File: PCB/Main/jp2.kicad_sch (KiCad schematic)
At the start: 1 part, among them U1 ORANGE_PI_CM4

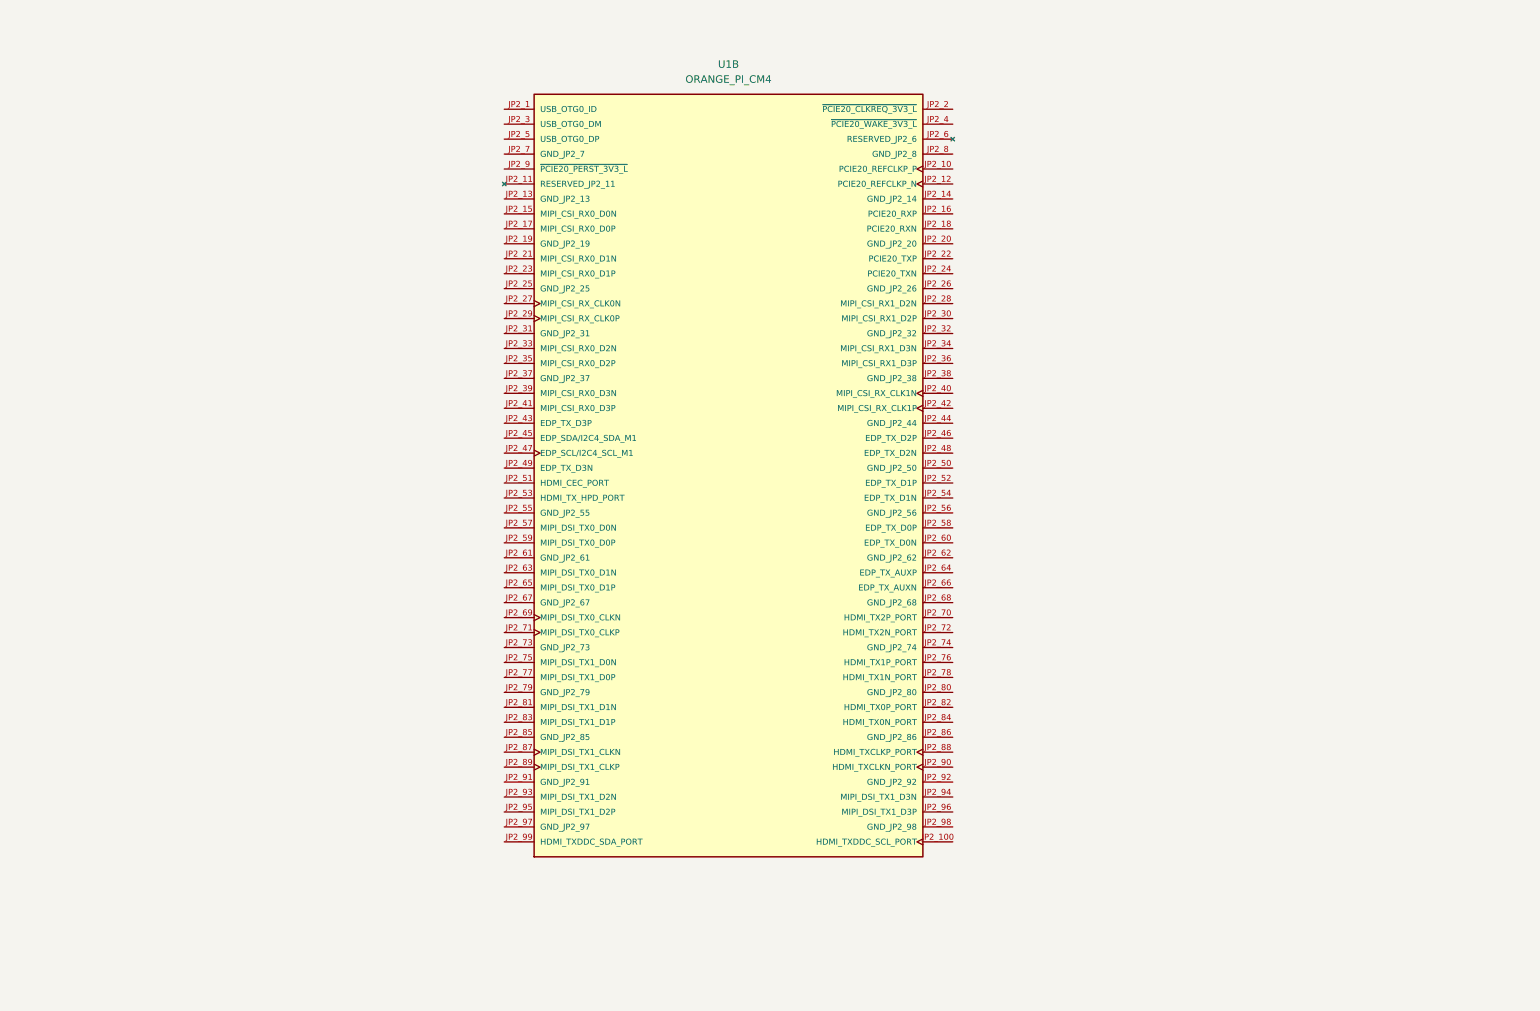
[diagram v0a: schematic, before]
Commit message: renaming y basico sin pcb
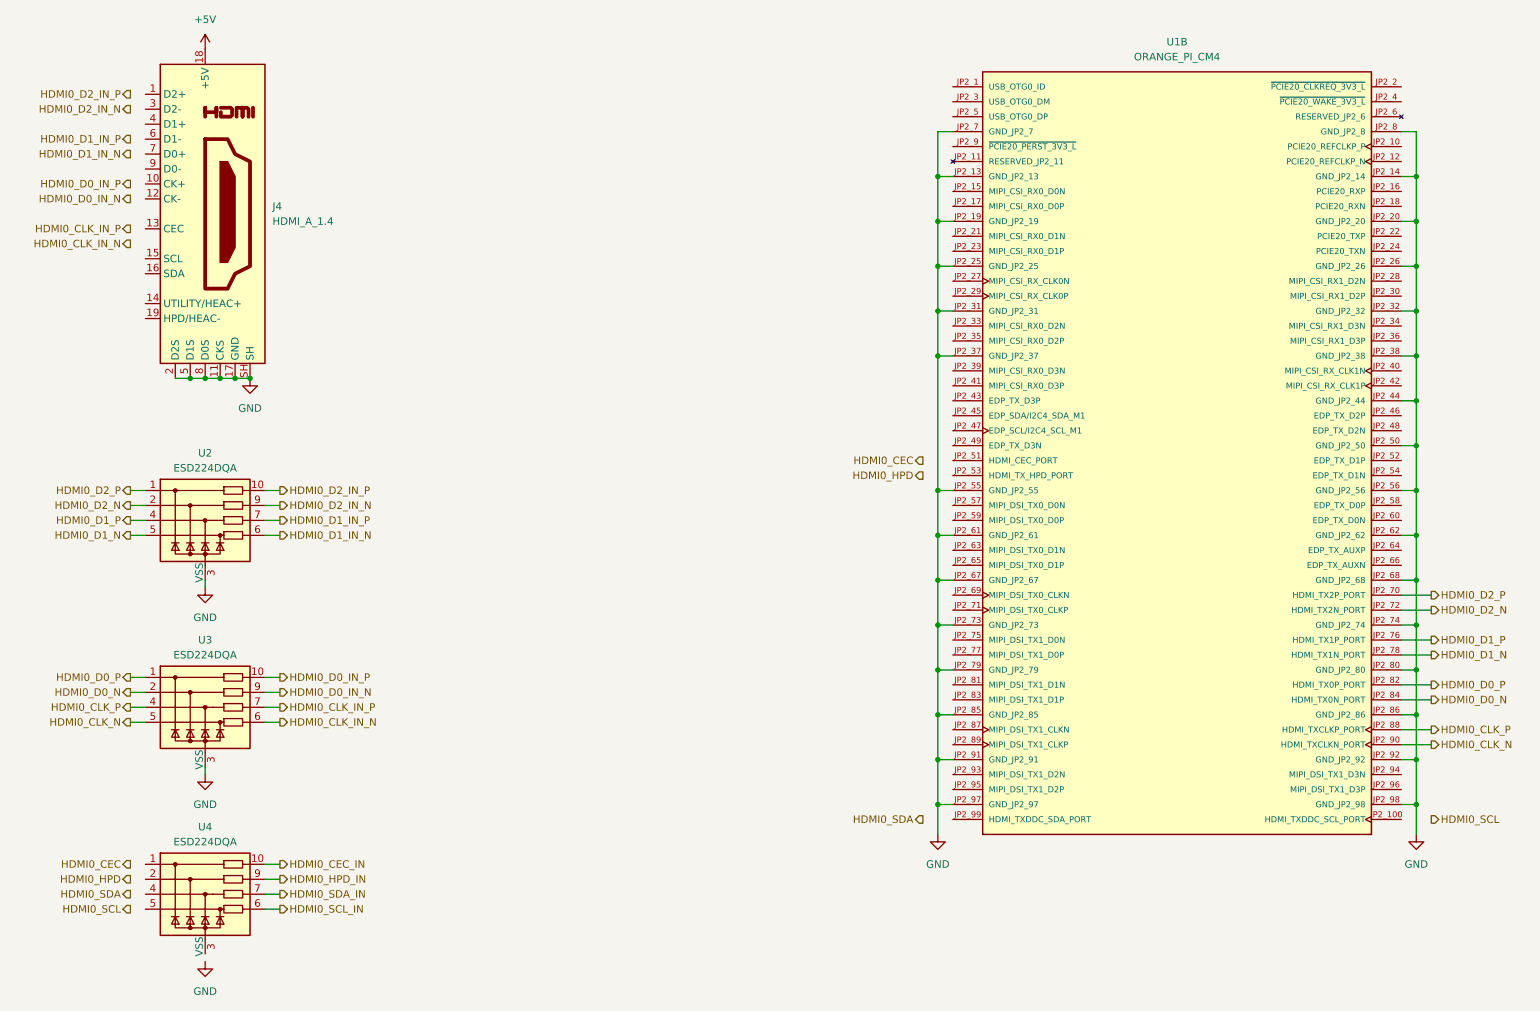
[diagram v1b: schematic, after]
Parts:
- added J4: HDMI_A_1.4, symbol Connector:HDMI_A_1.4
- added U2, U3, U4: ESD224DQA, Package_DFN_QFN:Diodes_UDFN-10_1x2.5mm_P0.5mm, symbol Power_Protection:ESD224DQA
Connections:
- net GND: now reaches U1.JP2_13 (GND_JP2_13)
- net GND: now also U1.JP2_14 (GND_JP2_14), U1.JP2_19 (GND_JP2_19), U1.JP2_20 (GND_JP2_20), U1.JP2_25 (GND_JP2_25), U1.JP2_26 (GND_JP2_26), U1.JP2_31 (GND_JP2_31), U1.JP2_32 (GND_JP2_32), U1.JP2_37 (GND_JP2_37), U1.JP2_38 (GND_JP2_38), U1.JP2_44 (GND_JP2_44), U1.JP2_50 (GND_JP2_50), U1.JP2_55 (GND_JP2_55), U1.JP2_56 (GND_JP2_56), U1.JP2_61 (GND_JP2_61), U1.JP2_62 (GND_JP2_62), U1.JP2_67 (GND_JP2_67), U1.JP2_68 (GND_JP2_68), U1.JP2_7 (GND_JP2_7), U1.JP2_73 (GND_JP2_73), U1.JP2_74 (GND_JP2_74), U1.JP2_79 (GND_JP2_79), U1.JP2_8 (GND_JP2_8), U1.JP2_80 (GND_JP2_80), U1.JP2_85 (GND_JP2_85), U1.JP2_86 (GND_JP2_86), U1.JP2_91 (GND_JP2_91), U1.JP2_92 (GND_JP2_92), U1.JP2_97 (GND_JP2_97), U1.JP2_98 (GND_JP2_98), J4.11 (CKS), J4.17 (GND), J4.2 (D2S), J4.5 (D1S), J4.8 (D0S), J4.SH, U2.3 (VSS), U2.8 (VSS), U3.3 (VSS), U3.8 (VSS)
- net HDMI0_D2_P: now reaches U1.JP2_70 (HDMI_TX2P_PORT)
- net HDMI0_D2_P: now also U2.1
- net HDMI0_D2_N: now reaches U1.JP2_72 (HDMI_TX2N_PORT)
- net HDMI0_D2_N: now also U2.2
- net HDMI0_D1_P: now reaches U1.JP2_76 (HDMI_TX1P_PORT)
- net HDMI0_D1_P: now also U2.4
- net HDMI0_D1_N: now reaches U1.JP2_78 (HDMI_TX1N_PORT)
- net HDMI0_D1_N: now also U2.5
- net HDMI0_D0_P: now reaches U1.JP2_82 (HDMI_TX0P_PORT)
- net HDMI0_D0_P: now also U3.1
- net HDMI0_D0_N: now reaches U1.JP2_84 (HDMI_TX0N_PORT)
- net HDMI0_D0_N: now also U3.2
- net HDMI0_CLK_P: now reaches U1.JP2_88 (HDMI_TXCLKP_PORT)
- net HDMI0_CLK_P: now also U3.4
- net HDMI0_CLK_N: now reaches U1.JP2_90 (HDMI_TXCLKN_PORT)
- net HDMI0_CLK_N: now also U3.5
- new net: U4.3 (VSS), U4.8 (VSS)
- new net +5V: J4.18 (+5V)
- new net HDMI0_CEC_IN: U4.10
- new net HDMI0_CLK_IN_N: U3.6
- new net HDMI0_CLK_IN_P: U3.7
- new net HDMI0_D0_IN_N: U3.9
- new net HDMI0_D0_IN_P: U3.10
- new net HDMI0_D1_IN_N: U2.6
- new net HDMI0_D1_IN_P: U2.7
- new net HDMI0_D2_IN_N: U2.9
- new net HDMI0_D2_IN_P: U2.10
- new net HDMI0_HPD_IN: U4.9
- new net HDMI0_SCL_IN: U4.6
- new net HDMI0_SDA_IN: U4.7
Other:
- moved on the sheet: U1B

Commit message: rename y conectores
tambien se añaden pours
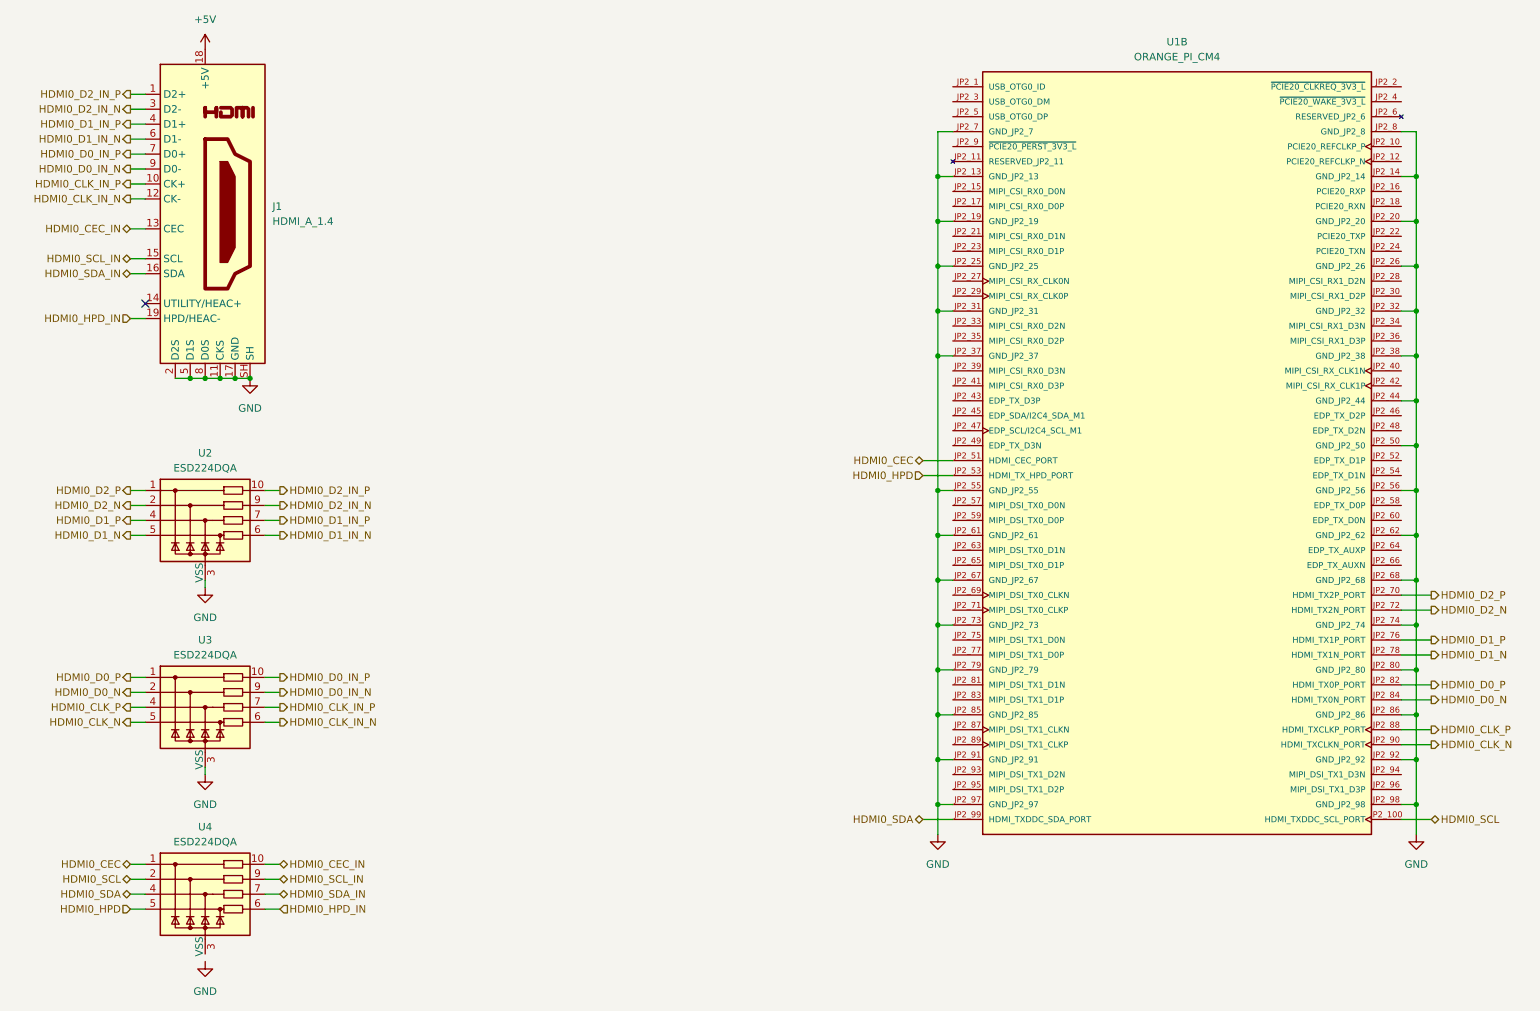
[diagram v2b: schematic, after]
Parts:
- J1: renamed from J4; footprint (none) -> Connector_Video:HDMI_A_Molex_208658-1001_Horizontal
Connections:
- net HDMI0_CEC: now also U1.JP2_51 (HDMI_CEC_PORT), U4.1
- net HDMI0_CEC_IN: now also J1.13 (CEC)
- net HDMI0_CLK_IN_N: now also J1.12 (CK-)
- net HDMI0_CLK_IN_P: now also J1.10 (CK+)
- net HDMI0_D0_IN_N: now also J1.9 (D0-)
- net HDMI0_D0_IN_P: now also J1.7 (D0+)
- net HDMI0_D1_IN_N: now also J1.6 (D1-)
- net HDMI0_D1_IN_P: now also J1.4 (D1+)
- net HDMI0_D2_IN_N: now also J1.3 (D2-)
- net HDMI0_D2_IN_P: now also J1.1 (D2+)
- net HDMI0_HPD: now also U1.JP2_53 (HDMI_TX_HPD_PORT), U4.5
- net HDMI0_HPD_IN: now also J1.19 (HPD/HEAC-), U4.6; no longer U4.9
- net HDMI0_SCL: now also U1.JP2_100 (HDMI_TXDDC_SCL_PORT), U4.2
- net HDMI0_SCL_IN: now also J1.15 (SCL), U4.9; no longer U4.6
- net HDMI0_SDA: now also U1.JP2_99 (HDMI_TXDDC_SDA_PORT), U4.4
- net HDMI0_SDA_IN: now also J1.16 (SDA)
- no-connect marks 0 -> 1
